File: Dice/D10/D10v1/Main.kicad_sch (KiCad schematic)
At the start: 28 parts, among them J1 Conn_01x14, J2 Conn_01x11, U1 N52810_QFN32, U2 KXTJ3-1057, Y1 32MHz 40ppm

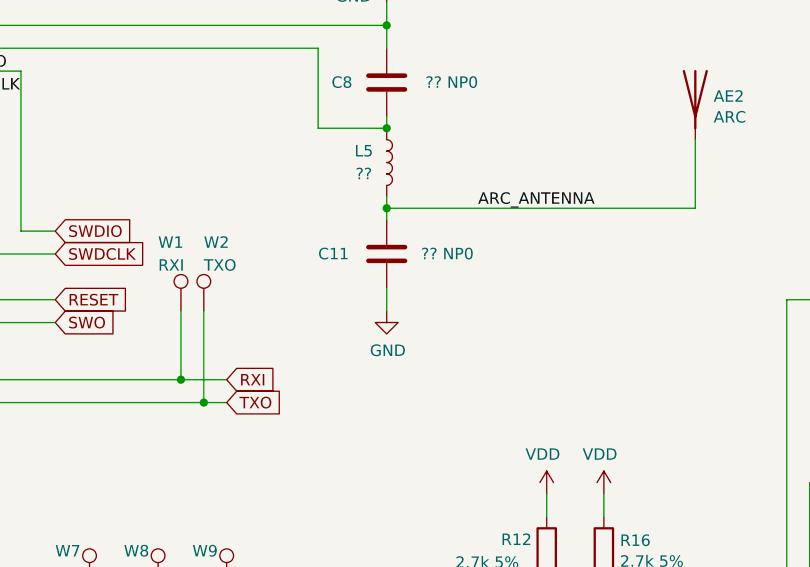
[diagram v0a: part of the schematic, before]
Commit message: Started work on D10 and fixed small mistakes in D6, PD6 and D12
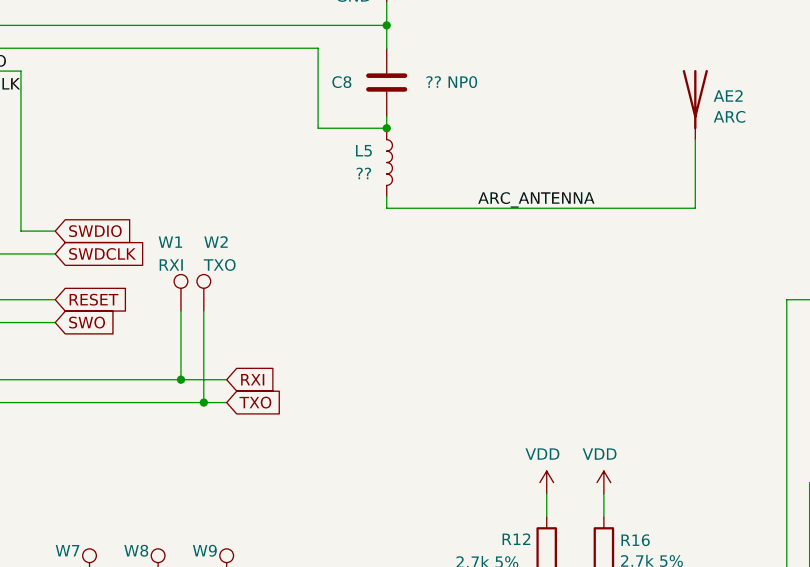
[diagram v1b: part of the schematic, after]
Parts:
- removed C11: ?? NP0, Capacitor_SMD:C_0402_1005Metric, symbol Device:C
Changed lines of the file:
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@@
   (junction (at 182.88 85.09) (diameter 0) (color 0 0 0 0)
-  )
-  (junction (at 182.88 105.41) (diameter 0) (color 0 0 0 0)
   )
   (junction (at 82.55 152.4) (diameter 0) (color 0 0 0 0)
@@
     (stroke (width 0) (type default) (color 0 0 0 0))
   )
-  (wire (pts (xy 182.88 105.41) (xy 182.88 106.68))
-    (stroke (width 0) (type default) (color 0 0 0 0))
-  )
   (wire (pts (xy 116.84 40.64) (xy 124.46 40.64))
     (stroke (width 0) (type default) (color 0 0 0 0))
@@
   )
   (wire (pts (xy 259.08 106.68) (xy 259.08 120.65))
-    (stroke (width 0) (type default) (color 0 0 0 0))
-  )
-  (wire (pts (xy 182.88 114.3) (xy 182.88 116.84))
     (stroke (width 0) (type default) (color 0 0 0 0))
   )
@@
     (pin "2")
   )
-  (symbol (lib_id "Device:C") (at 182.88 110.49 0) (unit 1)
-    (in_bom yes) (on_board yes)
-    (property "Reference" "C11" (id 0) (at 175.26 110.49 0)
-      (effects (font (size 1.27 1.27)) (justify left))
-    )
-    (property "Value" "?? NP0" (id 1) (at 186.69 110.49 0)
-      (effects (font (size 1.27 1.27)) (justify left))
-    )
-    (property "Footprint" "Capacitor_SMD:C_0402_1005Metric" (id 2) (at 183.8452 114.3 0)
-      (effects (font (size 1.27 1.27)) hide)
-    )
-    (property "Datasheet" "~" (id 3) (at 182.88 110.49 0)
-      (effects (font (size 1.27 1.27)) hide)
-    )
-    (property "Generic OK" "YES" (id 4) (at 182.88 110.49 0)
-      (effects (font (size 1.27 1.27)) hide)
-    )
-    (property "Pixels Part Number" "" (id 5) (at 182.88 110.49 0)
-      (effects (font (size 1.27 1.27)) hide)
-    )
-    (property "Manufacturer" "" (id 6) (at 182.88 110.49 0)
-      (effects (font (size 1.27 1.27)) hide)
-    )
-    (property "Manufacturer Part Number" "" (id 7) (at 182.88 110.49 0)
-      (effects (font (size 1.27 1.27)) hide)
-    )
-    (pin "1")
-    (pin "2")
-  )
   (symbol (lib_id "Device:Antenna") (at 217.17 92.71 0) (unit 1)
     (in_bom yes) (on_board yes)
@@
     )
     (property "Datasheet" "~" (id 3) (at 217.17 92.71 0)
-      (effects (font (size 1.27 1.27)) hide)
-    )
-    (pin "1")
-  )
-  (symbol (lib_id "power:GND") (at 182.88 116.84 0) (unit 1)
-    (in_bom yes) (on_board yes)
-    (property "Reference" "#PWR049" (id 0) (at 182.88 123.19 0)
-      (effects (font (size 1.27 1.27)) hide)
-    )
-    (property "Value" "GND" (id 1) (at 183.007 121.2342 0))
-    (property "Footprint" "" (id 2) (at 182.88 116.84 0)
-      (effects (font (size 1.27 1.27)) hide)
-    )
-    (property "Datasheet" "" (id 3) (at 182.88 116.84 0)
       (effects (font (size 1.27 1.27)) hide)
     )
@@
       (reference "#PWR048") (unit 1) (value "GND") (footprint "")
     )
-    (path "/00000000-0000-0000-0000-000061c0d6bd"
-      (reference "#PWR049") (unit 1) (value "GND") (footprint "")
-    )
     (path "/a0086b8f-a2d2-428c-9599-7d909b2bf8ec/9939dcb8-f9a9-4b62-ac89-9d3eafe84144"
       (reference "#PWR050") (unit 1) (value "GND") (footprint "")
@@
       (reference "#PWR0120") (unit 1) (value "GND") (footprint "")
     )
-    (path "/00000000-0000-0000-0000-00005bc88abf/00000000-0000-0000-0000-00005bd730bf"
-      (reference "#PWR0121") (unit 1) (value "VDC") (footprint "")
-    )
     (path "/00000000-0000-0000-0000-00005bc88abf/00000000-0000-0000-0000-00005bd730c5"
       (reference "#PWR0122") (unit 1) (value "GND") (footprint "")
     )
-    (path "/00000000-0000-0000-0000-00005bc88abf/00000000-0000-0000-0000-00005bd730cb"
-      (reference "#PWR0123") (unit 1) (value "GND") (footprint "")
-    )
-    (path "/00000000-0000-0000-0000-00005bc88abf/00000000-0000-0000-0000-00005bd730e3"
-      (reference "#PWR0124") (unit 1) (value "VDC") (footprint "")
-    )
-    (path "/00000000-0000-0000-0000-00005bc88abf/00000000-0000-0000-0000-00005bd7311b"
-      (reference "#PWR0129") (unit 1) (value "GND") (footprint "")
-    )
     (path "/00000000-0000-0000-0000-00005bc88abf/00000000-0000-0000-0000-00005bdeb14b"
       (reference "#PWR0140") (unit 1) (value "GND") (footprint "")
@@
       (reference "C10") (unit 1) (value "0.1uF 10V 20%") (footprint "Capacitor_SMD:C_0402_1005Metric")
     )
-    (path "/00000000-0000-0000-0000-000061c098e6"
-      (reference "C11") (unit 1) (value "?? NP0") (footprint "Capacitor_SMD:C_0402_1005Metric")
-    )
     (path "/a0086b8f-a2d2-428c-9599-7d909b2bf8ec/0fad7d6e-4a55-4fb0-bc91-a8854ff7ced8"
       (reference "C13") (unit 1) (value "4.7uF 25V 20%") (footprint "Capacitor_SMD:C_0603_1608Metric")
@@
       (reference "D11") (unit 1) (value "TX1812Z_2020") (footprint "Pixels-dice:TX1812Z_2020")
     )
-    (path "/00000000-0000-0000-0000-00005bc88abf/00000000-0000-0000-0000-000061431567"
-      (reference "D12") (unit 1) (value "TX1812Z_2020") (footprint "Pixels-dice:TX1812Z_2020")
-    )
-    (path "/00000000-0000-0000-0000-00005bc88abf/00000000-0000-0000-0000-0000614319e7"
-      (reference "D13") (unit 1) (value "TX1812Z_2020") (footprint "Pixels-dice:TX1812Z_2020")
-    )
     (path "/00000000-0000-0000-0000-00005c641b91"

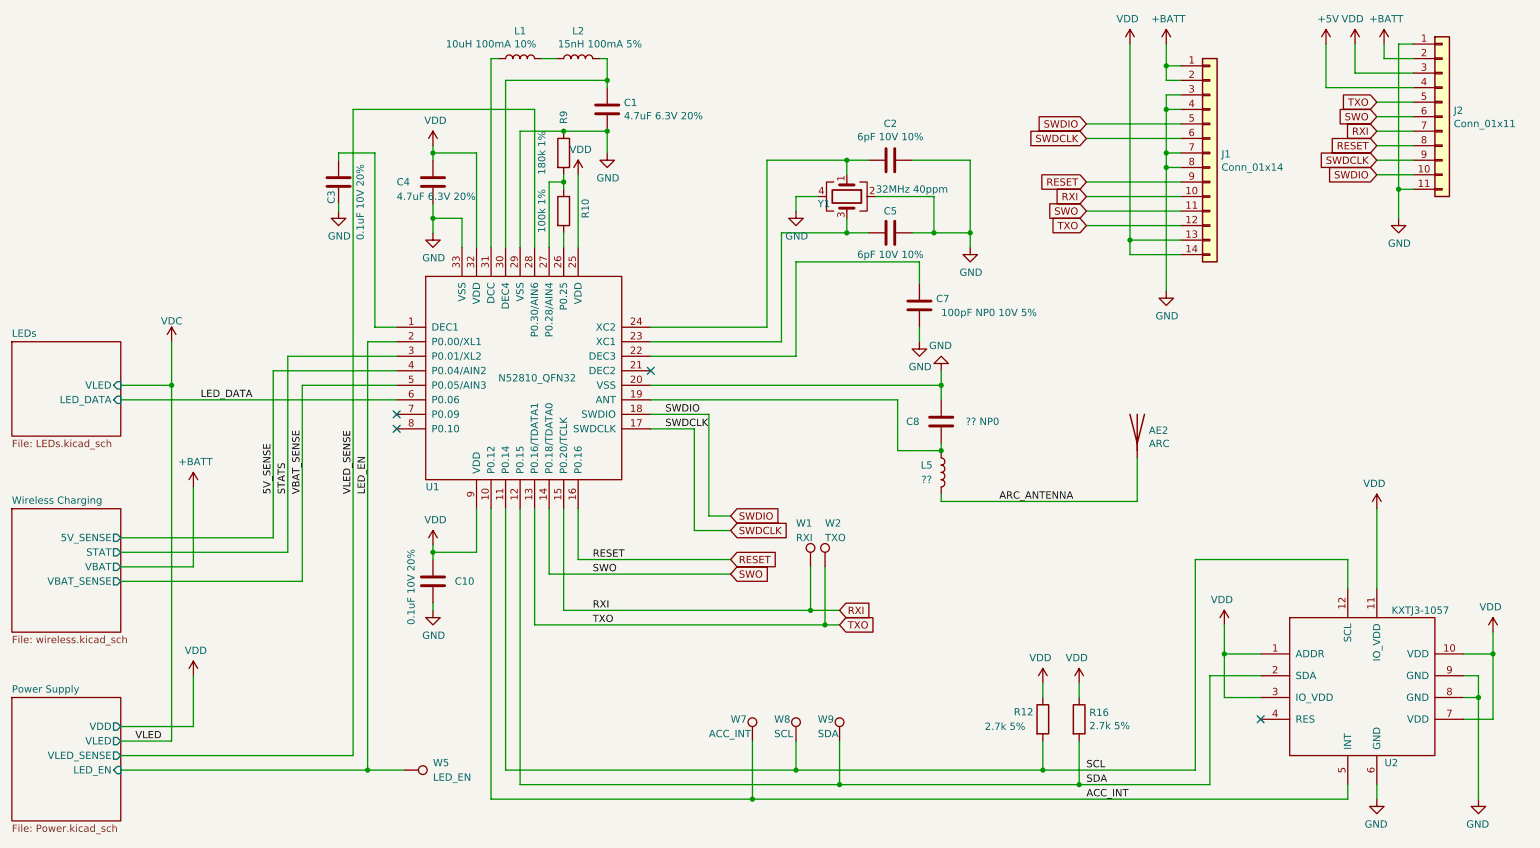
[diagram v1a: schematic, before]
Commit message: Added D10, D00 and D8, D20V12 updates
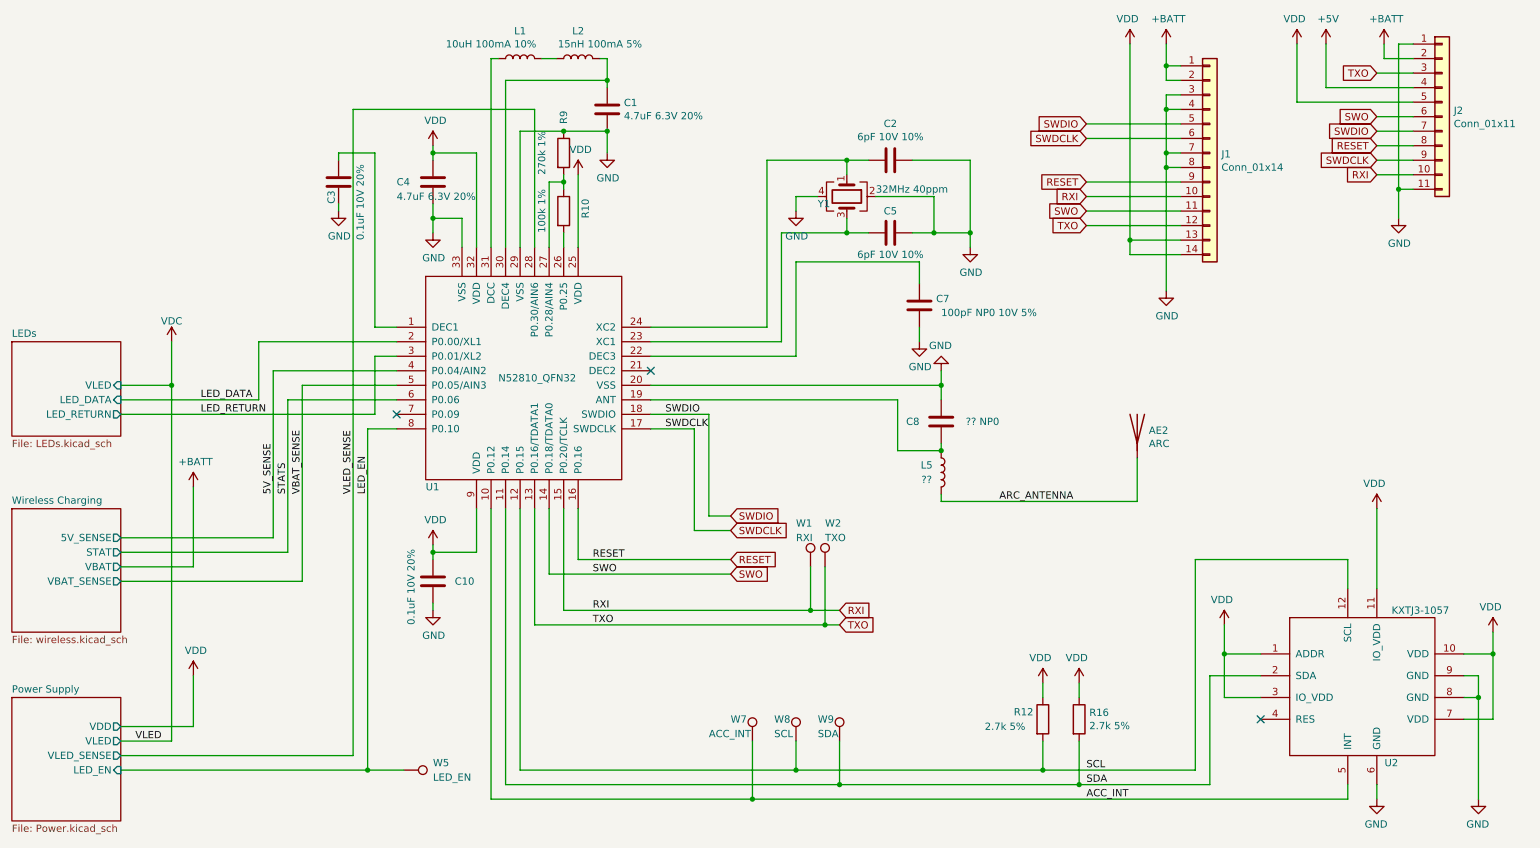
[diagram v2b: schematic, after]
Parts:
- R9: value 180k 1% -> 270k 1%
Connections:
- net LED_DATA: now also U1.2 (P0.00/XL1); no longer U1.6 (P0.06)
- net LED_EN: now also U1.8 (P0.10); no longer U1.2 (P0.00/XL1)
- net RXI: now also J2.10 (Pin_10); no longer J2.7 (Pin_7)
- net SCL: now also U1.12 (P0.15); no longer U1.11 (P0.14)
- net SDA: now also U1.11 (P0.14); no longer U1.12 (P0.15)
- net STATS: now also U1.6 (P0.06); no longer U1.3 (P0.01/XL2)
- net SWDIO: now also J2.7 (Pin_7); no longer J2.10 (Pin_10)
- net TXO: now also J2.3 (Pin_3); no longer J2.5 (Pin_5)
- net VDD: now also J2.5 (Pin_5); no longer J2.3 (Pin_3)
- new net LED_RETURN: U1.3 (P0.01/XL2)
- no-connect marks 4 -> 3
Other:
- sheet LEDs ports: added LED_RETURN; removed none
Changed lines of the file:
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@@
   (junction (at 166.37 45.72) (diameter 0) (color 0 0 0 0)
   )
-  (no_connect (at 87.63 92.71))
   (no_connect (at 132.08 82.55))
   (no_connect (at 87.63 90.17))
@@
     (stroke (width 0) (type default) (color 0 0 0 0))
   )
-  (wire (pts (xy 68.58 80.01) (xy 68.58 114.3))
-    (stroke (width 0) (type default) (color 0 0 0 0))
-  )
   (wire (pts (xy 154.94 77.47) (xy 154.94 58.42))
     (stroke (width 0) (type default) (color 0 0 0 0))
@@
     (stroke (width 0) (type default) (color 0 0 0 0))
   )
-  (wire (pts (xy 255.27 30.48) (xy 265.43 30.48))
-    (stroke (width 0) (type default) (color 0 0 0 0))
-  )
   (wire (pts (xy 132.08 87.63) (xy 175.26 87.63))
     (stroke (width 0) (type default) (color 0 0 0 0))
@@
     (stroke (width 0) (type default) (color 0 0 0 0))
   )
-  (wire (pts (xy 106.68 106.68) (xy 106.68 152.4))
-    (stroke (width 0) (type default) (color 0 0 0 0))
-  )
   (wire (pts (xy 182.88 104.14) (xy 182.88 105.41))
     (stroke (width 0) (type default) (color 0 0 0 0))
@@
     (stroke (width 0) (type default) (color 0 0 0 0))
   )
+  (wire (pts (xy 83.82 80.01) (xy 87.63 80.01))
+    (stroke (width 0) (type default) (color 0 0 0 0))
+  )
   (wire (pts (xy 254 120.65) (xy 254 115.57))
     (stroke (width 0) (type default) (color 0 0 0 0))
@@
     (stroke (width 0) (type default) (color 0 0 0 0))
   )
+  (wire (pts (xy 87.63 77.47) (xy 63.5 77.47))
+    (stroke (width 0) (type default) (color 0 0 0 0))
+  )
   (wire (pts (xy 222.25 44.45) (xy 222.25 46.99))
     (stroke (width 0) (type default) (color 0 0 0 0))
@@
     (stroke (width 0) (type default) (color 0 0 0 0))
   )
-  (wire (pts (xy 39.37 87.63) (xy 87.63 87.63))
-    (stroke (width 0) (type default) (color 0 0 0 0))
-  )
   (wire (pts (xy 123.19 27.94) (xy 124.46 27.94))
     (stroke (width 0) (type default) (color 0 0 0 0))
@@
     (stroke (width 0) (type default) (color 0 0 0 0))
   )
+  (wire (pts (xy 83.82 90.17) (xy 83.82 80.01))
+    (stroke (width 0) (type default) (color 0 0 0 0))
+  )
   (wire (pts (xy 222.25 36.83) (xy 222.25 44.45))
     (stroke (width 0) (type default) (color 0 0 0 0))
@@
     (stroke (width 0) (type default) (color 0 0 0 0))
   )
-  (wire (pts (xy 82.55 77.47) (xy 82.55 152.4))
-    (stroke (width 0) (type default) (color 0 0 0 0))
-  )
   (wire (pts (xy 200.66 137.16) (xy 200.66 139.7))
     (stroke (width 0) (type default) (color 0 0 0 0))
@@
     (stroke (width 0) (type default) (color 0 0 0 0))
   )
+  (wire (pts (xy 68.58 87.63) (xy 68.58 114.3))
+    (stroke (width 0) (type default) (color 0 0 0 0))
+  )
   (wire (pts (xy 262.89 55.88) (xy 262.89 50.8))
     (stroke (width 0) (type default) (color 0 0 0 0))
@@
     (stroke (width 0) (type default) (color 0 0 0 0))
   )
+  (wire (pts (xy 68.58 87.63) (xy 87.63 87.63))
+    (stroke (width 0) (type default) (color 0 0 0 0))
+  )
   (wire (pts (xy 152.4 45.72) (xy 166.37 45.72))
     (stroke (width 0) (type default) (color 0 0 0 0))
@@
     (stroke (width 0) (type default) (color 0 0 0 0))
   )
+  (wire (pts (xy 109.22 106.68) (xy 109.22 152.4))
+    (stroke (width 0) (type default) (color 0 0 0 0))
+  )
   (wire (pts (xy 39.37 119.38) (xy 71.12 119.38))
     (stroke (width 0) (type default) (color 0 0 0 0))
@@
     (stroke (width 0) (type default) (color 0 0 0 0))
   )
-  (wire (pts (xy 82.55 77.47) (xy 87.63 77.47))
-    (stroke (width 0) (type default) (color 0 0 0 0))
-  )
   (wire (pts (xy 200.66 152.4) (xy 227.33 152.4))
     (stroke (width 0) (type default) (color 0 0 0 0))
   )
-  (wire (pts (xy 109.22 154.94) (xy 165.1 154.94))
+  (wire (pts (xy 106.68 154.94) (xy 165.1 154.94))
     (stroke (width 0) (type default) (color 0 0 0 0))
   )
@@
     (stroke (width 0) (type default) (color 0 0 0 0))
   )
+  (wire (pts (xy 63.5 87.63) (xy 39.37 87.63))
+    (stroke (width 0) (type default) (color 0 0 0 0))
+  )
   (wire (pts (xy 87.63 82.55) (xy 66.04 82.55))
     (stroke (width 0) (type default) (color 0 0 0 0))
@@
     (stroke (width 0) (type default) (color 0 0 0 0))
   )
+  (wire (pts (xy 63.5 77.47) (xy 63.5 87.63))
+    (stroke (width 0) (type default) (color 0 0 0 0))
+  )
   (wire (pts (xy 104.14 27.94) (xy 105.41 27.94))
     (stroke (width 0) (type default) (color 0 0 0 0))
   )
+  (wire (pts (xy 106.68 154.94) (xy 106.68 106.68))
+    (stroke (width 0) (type default) (color 0 0 0 0))
+  )
   (wire (pts (xy 250.19 33.02) (xy 265.43 33.02))
     (stroke (width 0) (type default) (color 0 0 0 0))
@@
     (stroke (width 0) (type default) (color 0 0 0 0))
   )
-  (wire (pts (xy 87.63 80.01) (xy 68.58 80.01))
-    (stroke (width 0) (type default) (color 0 0 0 0))
-  )
   (wire (pts (xy 104.14 157.48) (xy 149.86 157.48))
     (stroke (width 0) (type default) (color 0 0 0 0))
@@
     (stroke (width 0) (type default) (color 0 0 0 0))
   )
+  (wire (pts (xy 82.55 92.71) (xy 87.63 92.71))
+    (stroke (width 0) (type default) (color 0 0 0 0))
+  )
   (wire (pts (xy 93.98 53.34) (xy 93.98 55.88))
     (stroke (width 0) (type default) (color 0 0 0 0))
@@
     (stroke (width 0) (type default) (color 0 0 0 0))
   )
-  (wire (pts (xy 255.27 25.4) (xy 255.27 30.48))
+  (wire (pts (xy 245.11 25.4) (xy 245.11 35.56))
     (stroke (width 0) (type default) (color 0 0 0 0))
   )
@@
     (stroke (width 0) (type default) (color 0 0 0 0))
   )
-  (wire (pts (xy 259.08 35.56) (xy 265.43 35.56))
+  (wire (pts (xy 245.11 35.56) (xy 265.43 35.56))
     (stroke (width 0) (type default) (color 0 0 0 0))
   )
@@
     (stroke (width 0) (type default) (color 0 0 0 0))
   )
+  (wire (pts (xy 39.37 90.17) (xy 83.82 90.17))
+    (stroke (width 0) (type default) (color 0 0 0 0))
+  )
   (wire (pts (xy 279.4 132.08) (xy 274.32 132.08))
     (stroke (width 0) (type default) (color 0 0 0 0))
@@
     (stroke (width 0) (type default) (color 0 0 0 0))
   )
-  (wire (pts (xy 109.22 106.68) (xy 109.22 154.94))
+  (wire (pts (xy 259.08 30.48) (xy 265.43 30.48))
     (stroke (width 0) (type default) (color 0 0 0 0))
   )
@@
     (stroke (width 0) (type default) (color 0 0 0 0))
   )
-  (wire (pts (xy 106.68 152.4) (xy 157.48 152.4))
+  (wire (pts (xy 82.55 92.71) (xy 82.55 152.4))
+    (stroke (width 0) (type default) (color 0 0 0 0))
+  )
+  (wire (pts (xy 109.22 152.4) (xy 157.48 152.4))
     (stroke (width 0) (type default) (color 0 0 0 0))
   )
@@
   )
   (label "VLED" (at 41.91 147.32 0)
+    (effects (font (size 1.27 1.27)) (justify left bottom))
+  )
+  (label "LED_RETURN" (at 53.34 90.17 0)
     (effects (font (size 1.27 1.27)) (justify left bottom))
   )
@@
     )
   )
-  (global_label "RXI" (shape input) (at 259.08 40.64 180) (fields_autoplaced)
+  (global_label "RXI" (shape input) (at 259.08 48.26 180) (fields_autoplaced)
     (effects (font (size 1.27 1.27)) (justify right))
-    (property "Intersheet References" "${INTERSHEET_REFS}" (id 0) (at 0 0 0)
+    (property "Intersheet References" "${INTERSHEET_REFS}" (id 0) (at 0 7.62 0)
       (effects (font (size 1.27 1.27)) hide)
     )
@@
     )
   )
-  (global_label "TXO" (shape input) (at 259.08 35.56 180) (fields_autoplaced)
+  (global_label "TXO" (shape input) (at 259.08 30.48 180) (fields_autoplaced)
     (effects (font (size 1.27 1.27)) (justify right))
-    (property "Intersheet References" "${INTERSHEET_REFS}" (id 0) (at 0 0 0)
+    (property "Intersheet References" "${INTERSHEET_REFS}" (id 0) (at 0 -5.08 0)
       (effects (font (size 1.27 1.27)) hide)
     )
@@
     )
   )
-  (global_label "SWDIO" (shape input) (at 259.08 48.26 180) (fields_autoplaced)
+  (global_label "SWDIO" (shape input) (at 259.08 40.64 180) (fields_autoplaced)
     (effects (font (size 1.27 1.27)) (justify right))
-    (property "Intersheet References" "${INTERSHEET_REFS}" (id 0) (at 0 0 0)
+    (property "Intersheet References" "${INTERSHEET_REFS}" (id 0) (at 0 -7.62 0)
       (effects (font (size 1.27 1.27)) hide)
     )
@@
       (effects (font (size 1.27 1.27)) (justify left))
     )
-    (property "Value" "180k 1%" (id 1) (at 113.03 48.26 90)
+    (property "Value" "270k 1%" (id 1) (at 113.03 48.26 90)
       (effects (font (size 1.27 1.27)) (justify left))
     )
@@
     (pin "1")
   )
-  (symbol (lib_id "power:VDD") (at 255.27 25.4 0) (mirror y) (unit 1)
-    (in_bom yes) (on_board yes)
-    (property "Reference" "#PWR018" (id 0) (at 255.27 29.21 0)
-      (effects (font (size 1.27 1.27)) hide)
-    )
-    (property "Value" "VDD" (id 1) (at 254.8382 21.0058 0))
-    (property "Footprint" "" (id 2) (at 255.27 25.4 0)
-      (effects (font (size 1.27 1.27)) hide)
-    )
-    (property "Datasheet" "" (id 3) (at 255.27 25.4 0)
+  (symbol (lib_id "power:VDD") (at 245.11 25.4 0) (mirror y) (unit 1)
+    (in_bom yes) (on_board yes)
+    (property "Reference" "#PWR018" (id 0) (at 245.11 29.21 0)
+      (effects (font (size 1.27 1.27)) hide)
+    )
+    (property "Value" "VDD" (id 1) (at 244.6782 21.0058 0))
+    (property "Footprint" "" (id 2) (at 245.11 25.4 0)
+      (effects (font (size 1.27 1.27)) hide)
+    )
+    (property "Datasheet" "" (id 3) (at 245.11 25.4 0)
       (effects (font (size 1.27 1.27)) hide)
     )
@@
       (effects (font (size 1.27 1.27)) (justify right))
     )
+    (pin "LED_RETURN" output (at 39.37 90.17 0)
+      (effects (font (size 1.27 1.27)) (justify right))
+    )
   )
   (sheet (at 20.32 106.68) (size 19.05 21.59) (fields_autoplaced)
@@
     )
     (path "/00000000-0000-0000-0000-00005cbb0f24"
-      (reference "R9") (unit 1) (value "180k 1%") (footprint "Resistor_SMD:R_0402_1005Metric")
+      (reference "R9") (unit 1) (value "270k 1%") (footprint "Resistor_SMD:R_0402_1005Metric")
     )
     (path "/00000000-0000-0000-0000-00005cbb0c6c"
